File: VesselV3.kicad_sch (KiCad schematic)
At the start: 389 parts, among them IC1 USB3320C-EZK-TR, IC3 5VOutput_VoltageRegulator, IC4 BidirectionalLogicLevelShifter, IC6 AND Gate, J1 JTAG/SWD 10pins Headers, Y1 25MHz

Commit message: Initial PCB Board Setup
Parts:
- added C40: 0.1uF, SamacSys_Parts:CAPC1005X55N, symbol SamacSys_Parts:GRM155R71A104JA01D
- IC6: footprint SOT65P212X110-5N -> SamacSys_Parts:SOT65P212X110-5N
- LED1, LED10, LED100, LED101, LED102, LED11, LED12, LED13, LED14, LED15, LED16, LED17, LED18, LED19, LED2, LED20, LED21, LED22, LED23, LED24, LED25, LED26, LED27, LED28, LED29, LED3, LED30, LED31, LED32, LED33, LED34, LED35, LED36, LED37, LED38, LED39, LED4, LED40, LED41, LED42, LED43, LED44, LED45, LED46, LED47, LED48, LED49, LED5, LED50, LED51, LED52, LED53, LED54, LED55, LED56, LED57, LED58, LED59, LED6, LED60, LED61, LED62, LED63, LED64, LED65, LED66, LED67, LED68, LED69, LED7, LED70, LED71, LED72, LED73, LED74, LED75, LED76, LED77, LED78, LED79, LED8, LED80, LED81, LED82, LED83, LED84, LED85, LED86, LED87, LED88, LED89, LED9, LED90, LED91, LED92, LED93, LED94, LED95, LED96, LED97, LED98, LED99: footprint 4684_ADA -> WS2812BNano4684RGB-3rdParty:4684_ADA
- PNPTransistor1: footprint BC55PASQX -> SamacSys_Parts:BC55PASQX
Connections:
- net +1V8: now also C40.1
- net GND: now also C40.2
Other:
- moved on the sheet: C24, C33

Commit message: PCB layout - Initial Commit
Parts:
- added C41: 0.01u, SamacSys_Parts:CAPC1005X56N, symbol SamacSys_Parts:0402ZC103JAT2A
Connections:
- net GND: now also C41.1
- net ROTARY-ENC_PUSH: now also C41.2
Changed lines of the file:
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@@
   (junction (at 172.72 101.6) (diameter 0) (color 0 0 0 0)
   )
+  (junction (at 570.23 257.81) (diameter 0) (color 0 0 0 0)
+  )
   (junction (at 66.04 132.08) (diameter 0) (color 0 0 0 0)
   )
@@
     (stroke (width 0) (type default))
   )
+  (wire (pts (xy 565.15 257.81) (xy 570.23 257.81))
+    (stroke (width 0) (type default))
+  )
   (wire (pts (xy 177.8 403.86) (xy 226.06 403.86))
     (stroke (width 0) (type default))
@@
     )
   )
-  (global_label "ROTARY-ENC_PUSH" (shape input) (at 570.23 257.81 180) (fields_autoplaced)
+  (global_label "ROTARY-ENC_PUSH" (shape input) (at 565.15 257.81 180) (fields_autoplaced)
     (effects (font (size 1.27 1.27)) (justify right))
-    (property "Intersheetrefs" "${INTERSHEET_REFS}" (at 548.7995 257.81 0)
+    (property "Intersheetrefs" "${INTERSHEET_REFS}" (at 543.7195 257.81 0)
       (effects (font (size 1.27 1.27)) (justify right) hide)
     )
@@
     )
   )
+  (symbol (lib_id "SamacSys_Parts:0402ZC103JAT2A") (at 570.23 270.51 90) (unit 1)
+    (in_bom yes) (on_board yes) (dnp no)
+    (property "Reference" "C41" (at 567.69 265.43 90)
+      (effects (font (size 1.27 1.27)) (justify left))
+    )
+    (property "Value" "0.01u" (at 567.69 262.89 90)
+      (effects (font (size 1.27 1.27)) (justify left))
+    )
+    (property "Footprint" "SamacSys_Parts:CAPC1005X56N" (at 666.42 261.62 0)
+      (effects (font (size 1.27 1.27)) (justify left top) hide)
+    )
+    (property "Datasheet" "https://www.mouser.com/datasheet/2/40/KGM_X7R-3223212.pdf" (at 766.42 261.62 0)
+      (effects (font (size 1.27 1.27)) (justify left top) hide)
+    )
+    (property "Height" "0.56" (at 966.42 261.62 0)
+      (effects (font (size 1.27 1.27)) (justify left top) hide)
+    )
+    (property "Mouser Part Number" "581-0402ZC103JAT2A" (at 1066.42 261.62 0)
+      (effects (font (size 1.27 1.27)) (justify left top) hide)
+    )
+    (property "Mouser Price/Stock" "https://www.mouser.co.uk/ProductDetail/AVX/0402ZC103JAT2A?qs=ELahxSJG%252B8HAL%252BImKS119Q%3D%3D" (at 1166.42 261.62 0)
+      (effects (font (size 1.27 1.27)) (justify left top) hide)
+    )
+    (property "Manufacturer_Name" "AVX" (at 1266.42 261.62 0)
+      (effects (font (size 1.27 1.27)) (justify left top) hide)
+    )
+    (property "Manufacturer_Part_Number" "0402ZC103JAT2A" (at 1366.42 261.62 0)
+      (effects (font (size 1.27 1.27)) (justify left top) hide)
+    )
+    (property "DigikeyPartNumber" "478-KGM05AR71A103JHTR-ND" (at 570.23 270.51 0)
+      (effects (font (size 1.27 1.27)) hide)
+    )
+    (property "Sim.Device" "C" (at 570.23 270.51 0)
+      (effects (font (size 1.27 1.27)) hide)
+    )
+    (property "Sim.Pins" "1=+ 2=-" (at 570.23 270.51 0)
+      (effects (font (size 1.27 1.27)) hide)
+    )
+    (pin "1")
+    (pin "2")
+    (instances
+      (project "VesselV3"
+        (path "/7364f6a3-b999-47c8-8f6d-f83e5421d1ed"
+          (reference "C41") (unit 1)
+        )
+      )
+    )
+  )
   (symbol (lib_id "Device:D_Small") (at 113.03 76.2 90) (unit 1)
     (in_bom yes) (on_board yes) (dnp no) (fields_autoplaced)
@@
         )
       )
+    )
+  )
+  (symbol (lib_id "power:GND") (at 570.23 270.51 0) (unit 1)
+    (in_bom yes) (on_board yes) (dnp no) (fields_autoplaced)
+    (property "Reference" "#PWR083" (at 570.23 276.86 0)
+      (effects (font (size 1.27 1.27)) hide)
+    )
+    (property "Value" "GND" (at 570.23 275.59 0)
+      (effects (font (size 1.27 1.27)))
+    )
+    (property "Footprint" "" (at 570.23 270.51 0)
+      (effects (font (size 1.27 1.27)) hide)
+    )
+    (property "Datasheet" "" (at 570.23 270.51 0)
+      (effects (font (size 1.27 1.27)) hide)
+    )
+    (pin "1")
+    (instances
+      (project "VesselV3"
+        (path "/7364f6a3-b999-47c8-8f6d-f83e5421d1ed"
+          (reference "#PWR083") (unit 1)
+        )
+      )

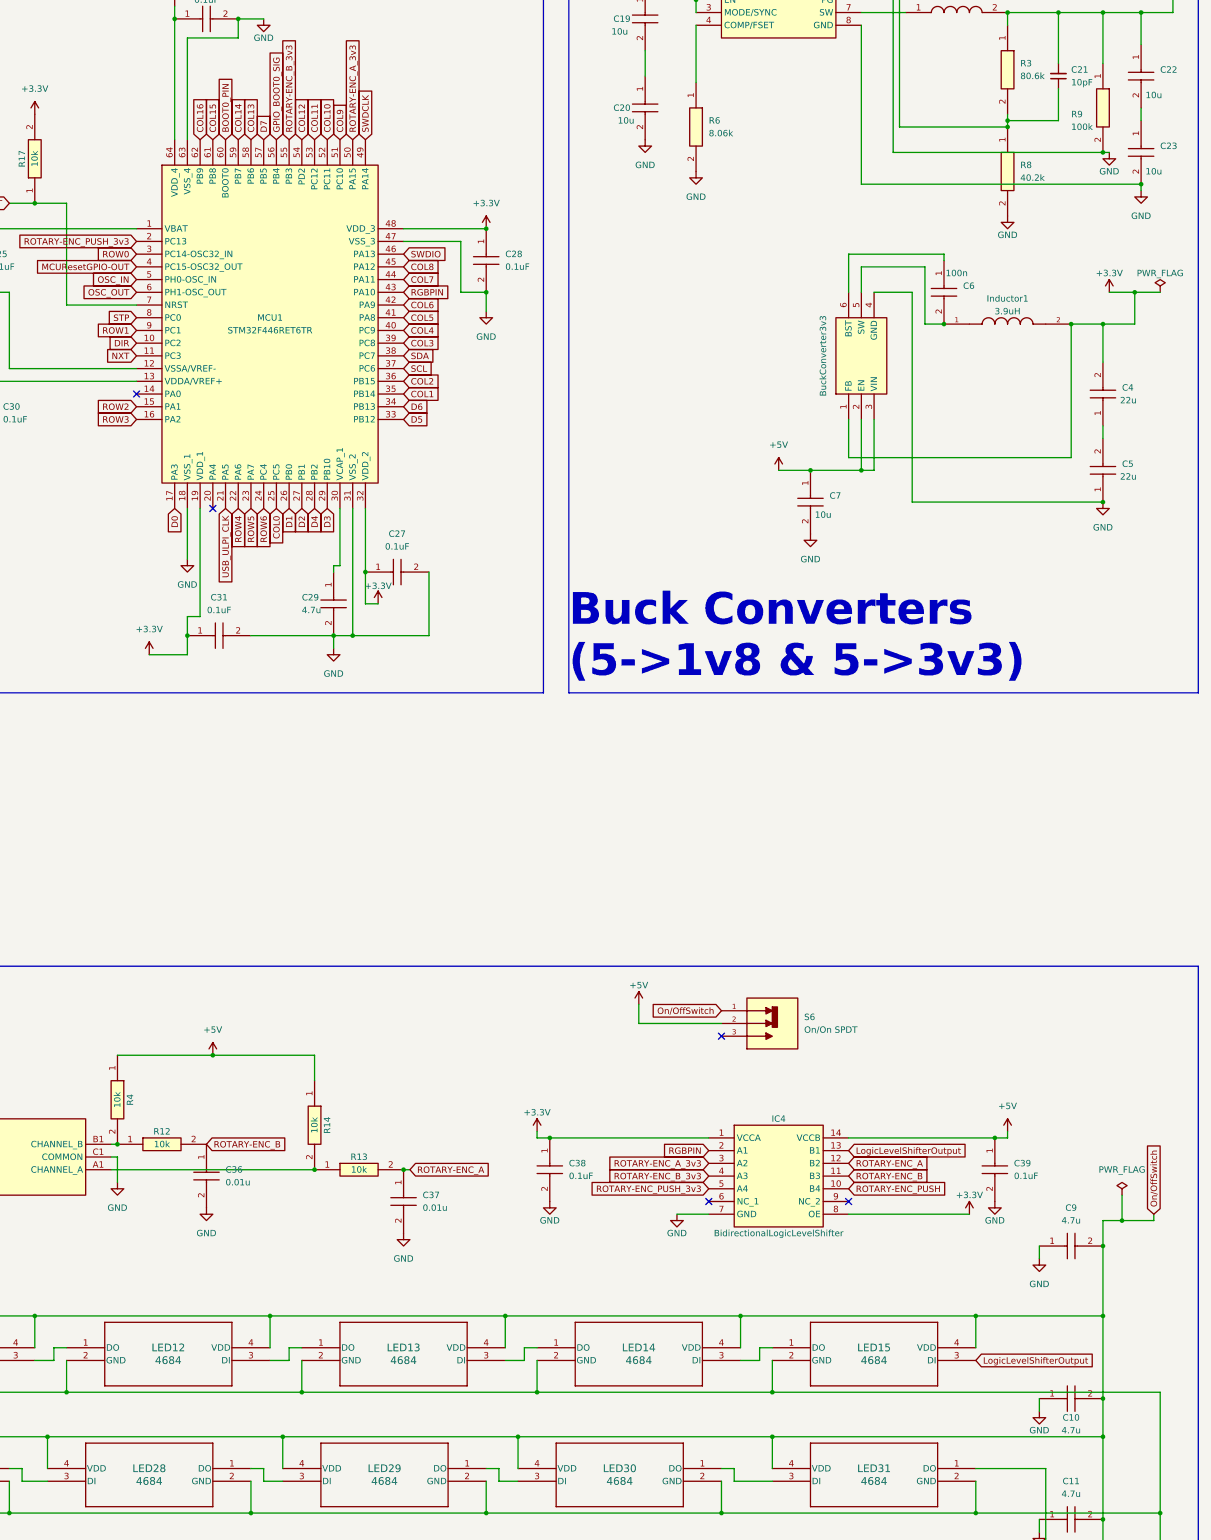
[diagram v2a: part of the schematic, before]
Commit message: Rough PCB Layout and GPIO Pins Swaps
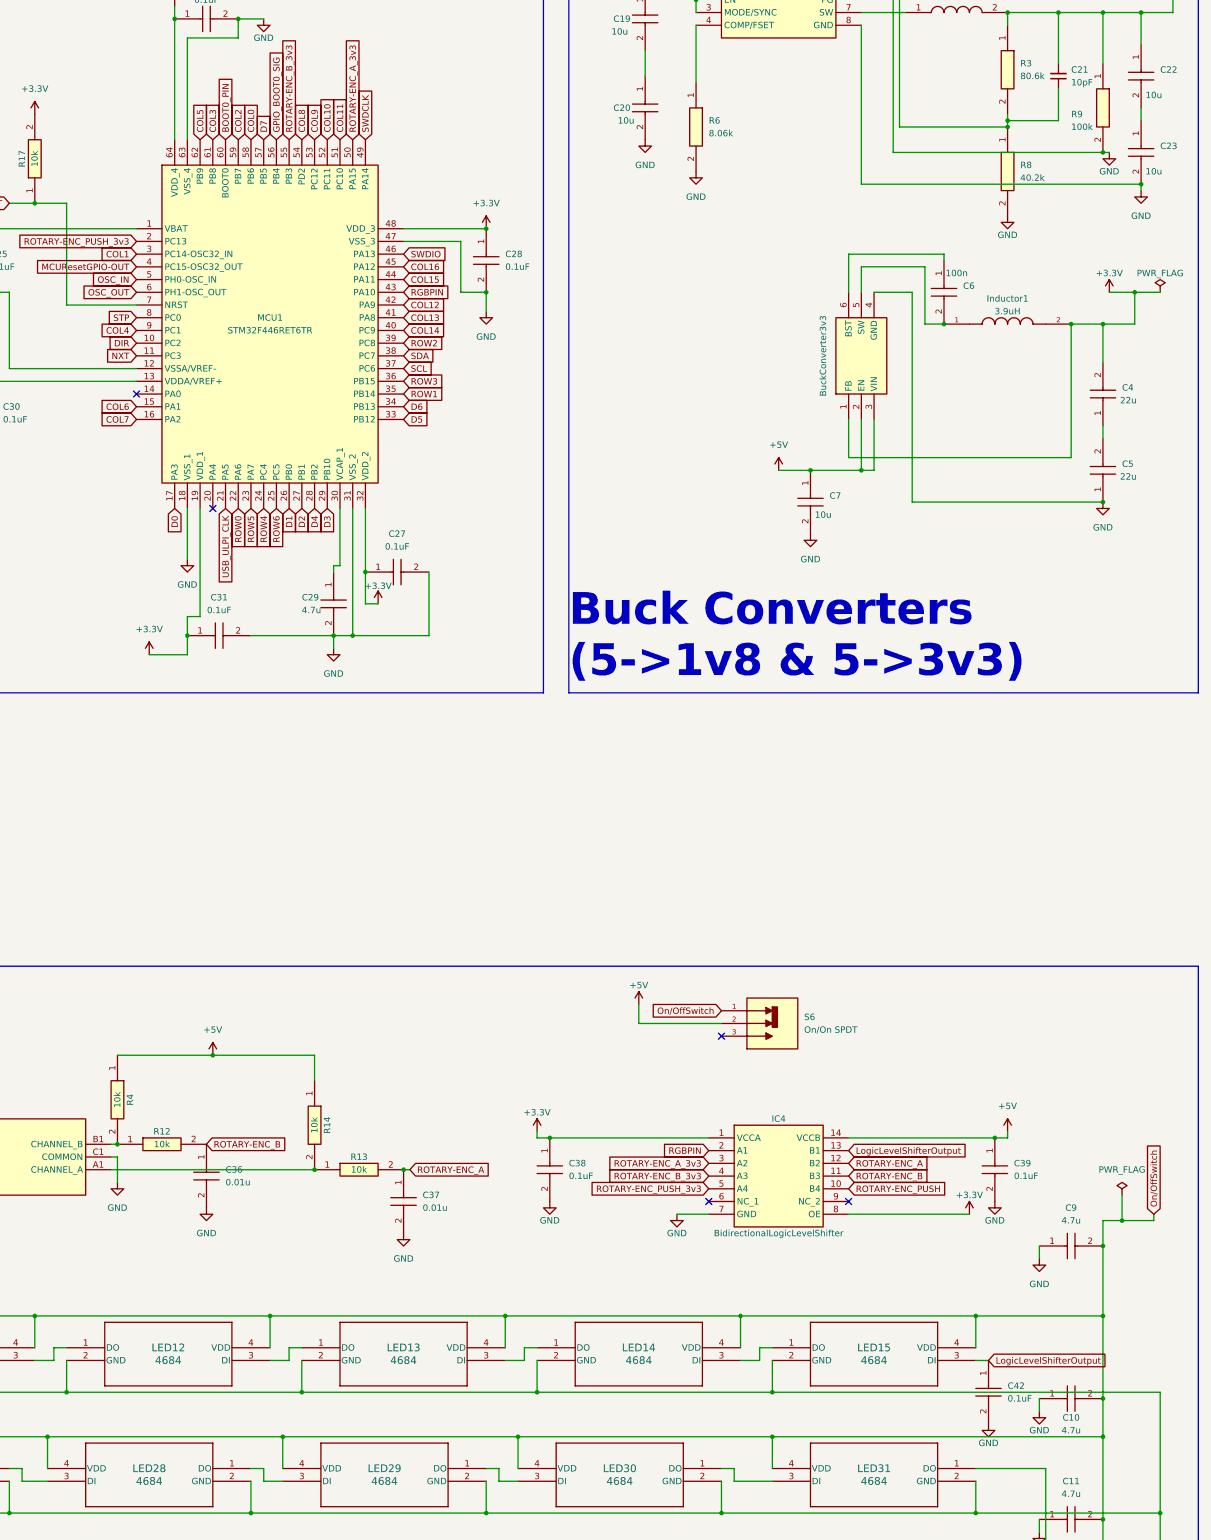
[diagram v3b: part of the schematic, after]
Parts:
- added C42: 0.1uF, SamacSys_Parts:CAPC1005X55N, symbol SamacSys_Parts:GRM155R71A104JA01D
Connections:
- net COL0: now also MCU1.58 (PB6); no longer MCU1.25 (PC5)
- net COL1: now also MCU1.3 (PC14-OSC32_IN); no longer MCU1.35 (PB14)
- net COL11: now also MCU1.51 (PC10); no longer MCU1.53 (PC12)
- net COL12: now also MCU1.42 (PA9); no longer MCU1.54 (PD2)
- net COL13: now also MCU1.41 (PA8); no longer MCU1.58 (PB6)
- net COL14: now also MCU1.40 (PC9); no longer MCU1.59 (PB7)
- net COL15: now also MCU1.44 (PA11); no longer MCU1.61 (PB8)
- net COL16: now also MCU1.45 (PA12); no longer MCU1.62 (PB9)
- net COL2: now also MCU1.59 (PB7); no longer MCU1.36 (PB15)
- net COL3: now also MCU1.61 (PB8); no longer MCU1.39 (PC8)
- net COL4: now also MCU1.9 (PC1); no longer MCU1.40 (PC9)
- net COL5: now also MCU1.62 (PB9); no longer MCU1.41 (PA8)
- net COL6: now also MCU1.15 (PA1); no longer MCU1.42 (PA9)
- net COL7: now also MCU1.16 (PA2); no longer MCU1.44 (PA11)
- net COL8: now also MCU1.54 (PD2); no longer MCU1.45 (PA12)
- net COL9: now also MCU1.53 (PC12); no longer MCU1.51 (PC10)
- net GND: now also C42.2
- net LogicLevelShifterOutput: now also C42.1
- net ROW0: now also MCU1.22 (PA6); no longer MCU1.3 (PC14-OSC32_IN)
- net ROW1: now also MCU1.35 (PB14); no longer MCU1.9 (PC1)
- net ROW2: now also MCU1.39 (PC8); no longer MCU1.15 (PA1)
- net ROW3: now also MCU1.36 (PB15); no longer MCU1.16 (PA2)
- net ROW4: now also MCU1.24 (PC4); no longer MCU1.22 (PA6)
- net ROW6: now also MCU1.25 (PC5); no longer MCU1.24 (PC4)

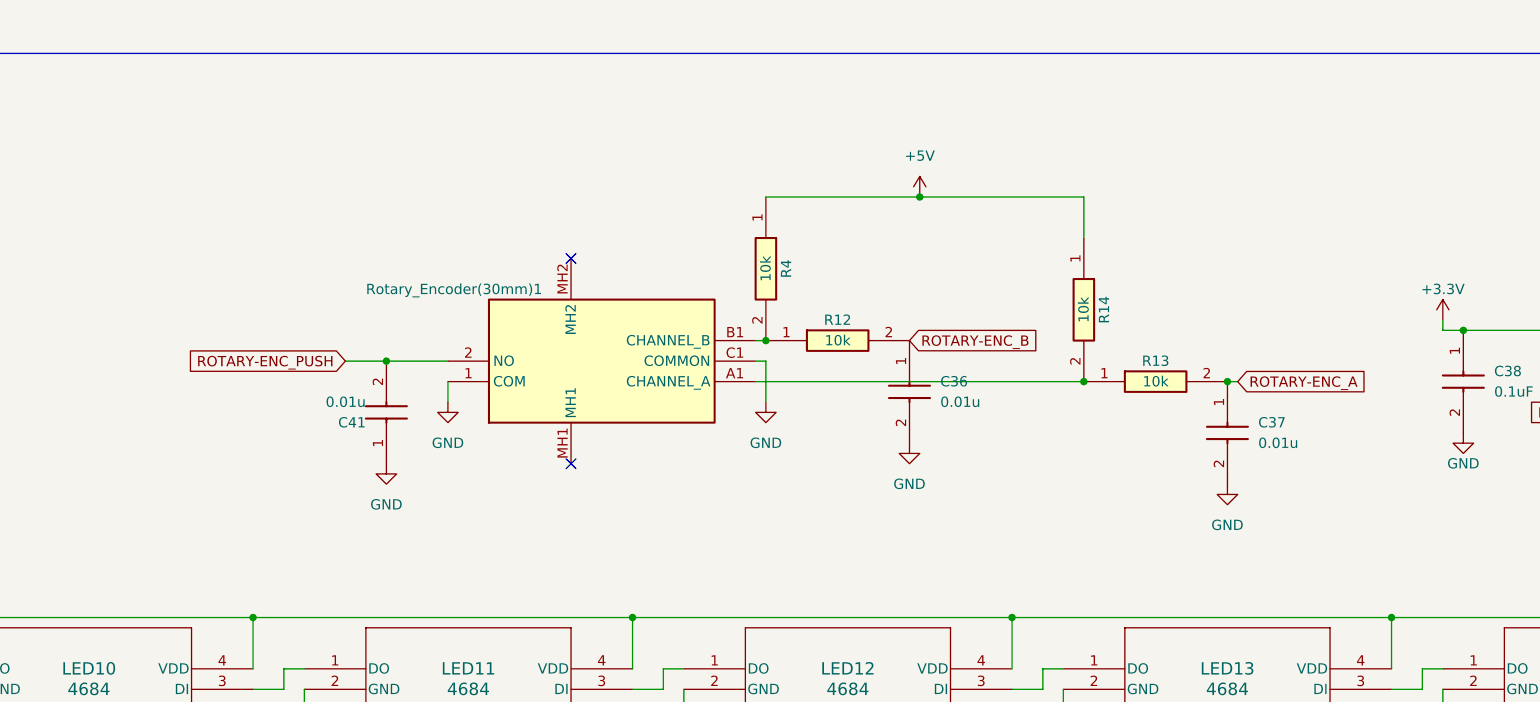
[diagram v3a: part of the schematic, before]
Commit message: Swapped encoder for smaller one
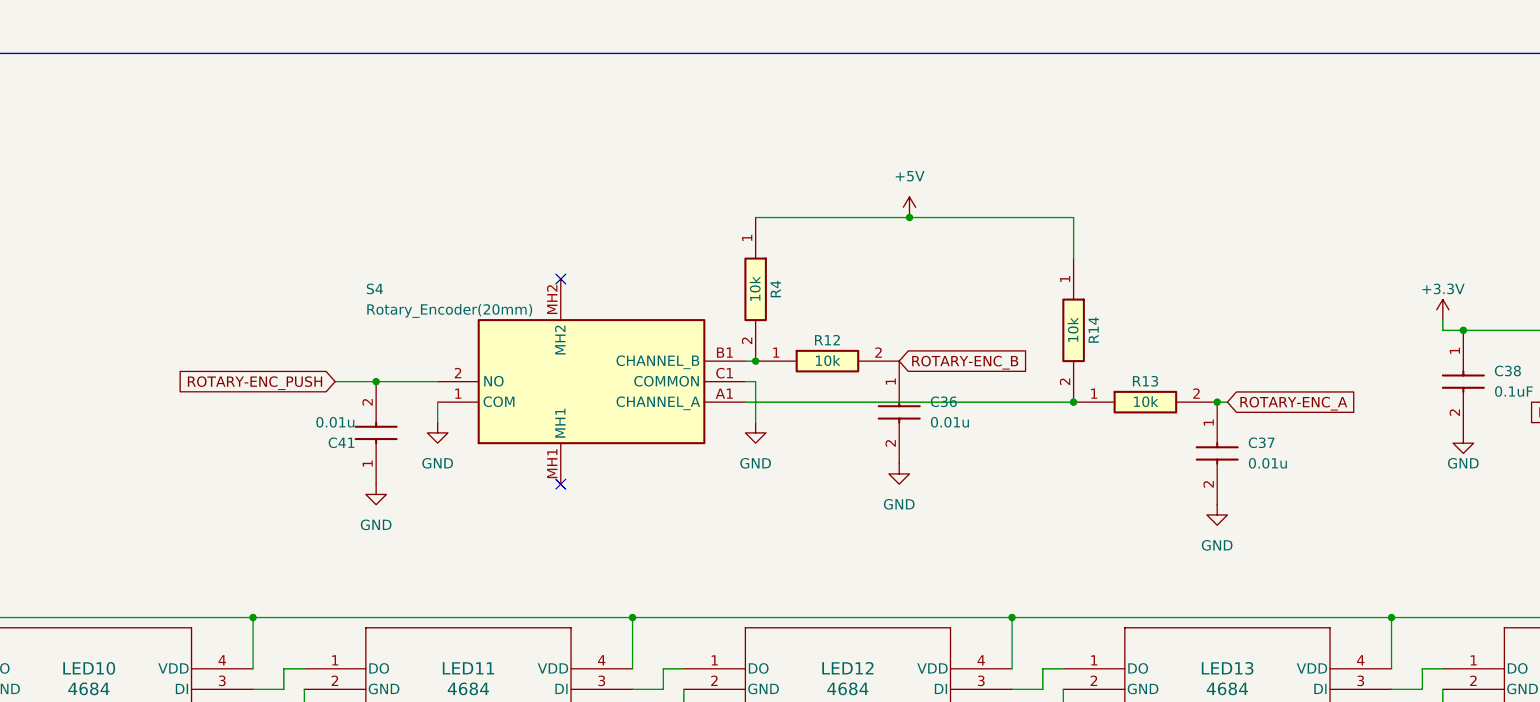
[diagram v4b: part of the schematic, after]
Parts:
- removed Rotary_Encoder(30mm)1: PEC12R-4230F-S0024, SamacSys_Parts:PEC12R4230FS0024, symbol SamacSys_Parts:PEC12R-4230F-S0024
- added S4: Rotary_Encoder(20mm), PEC12R3220FS0024, symbol SamacSys_Parts:PEC12R-3220F-S0024
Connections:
- net GND: now also S4.1 (COM), S4.C1 (COMMON)
- net ROTARY-ENC_PUSH: now also S4.2 (NO)
- net at R13.1, R14.2: now also S4.A1 (CHANNEL_A)
- net at R12.1, R4.2: now also S4.B1 (CHANNEL_B)
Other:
- moved on the sheet: C36, C37, C41, R12, R13, R14, R4

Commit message: Fully Routed PCB
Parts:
- removed C1, C2: 20pF, SamacSys_Parts:C0805, symbol SamacSys_Parts:C0805C200G8HACTU
- added C1, C2: 20pF, SamacSys_Parts:C0603, symbol SamacSys_Parts:C0603C200G8HACTU
- added H1, H2, H3, H4: MountingHole, MountingHole:MountingHole_2.5mm_Pad_Via, symbol Mechanical:MountingHole
- S4: footprint PEC12R3220FS0024 -> SamacSys_Parts:PEC12R3220FS0024
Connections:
- net GND: now also C1.1, C2.1; no longer USB-C1.MH3, USB-C1.MH4, USB-C1.MH5, USB-C1.MH6
- net OSC_IN: now also C1.2
- net at R10.1, Y1.2 (X2): now also C2.2
- no-connect marks 19 -> 23
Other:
- note added: "Mounting Holes"
